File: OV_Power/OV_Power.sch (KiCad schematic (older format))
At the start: 41 parts, among them Q1 SSM3K341R, Q2 2N7002BK, U1 LT3796, U2 LT1936

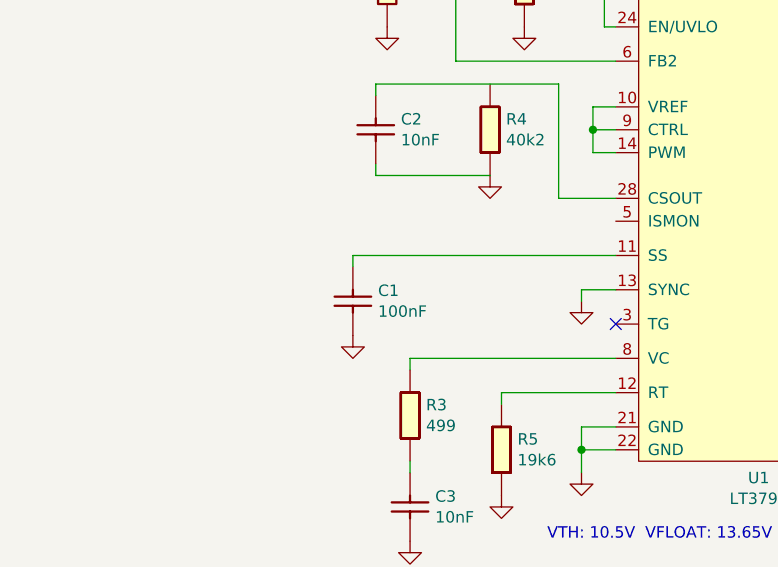
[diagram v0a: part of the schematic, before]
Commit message: Sorted out the interconnect between power supply and main boards.
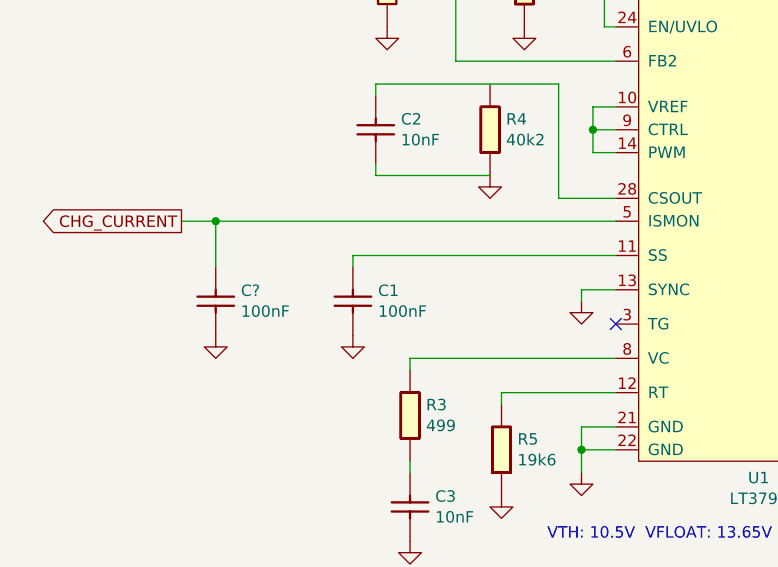
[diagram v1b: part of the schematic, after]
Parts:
- added C?: 100nF_0603_Ceramic_Capacitor,_10%,_X7R,_25V, Capacitor_SMD:C_0603_1608Metric, symbol OpenVent:100nF_0603_Ceramic_Capacitor,_10%,_X7R,_25V
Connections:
- net labels added: CHG_CURRENT
- wire segments 149 -> 152
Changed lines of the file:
@@
 Text Notes 10300 2000 0    50   ~ 0
 NEED CONNECTOR\nDEFINITION FOR\nGELL CELL.\nTHIS CONNECTION\nALSO NEEDS TO\nBE FUSED.
+$Comp
+L OpenVent:100nF_0603_Ceramic_Capacitor,_10%,_X7R,_25V C?
+U 1 1 5FB9582D
+P 2450 3100
+F 0 "C?" V 2454 3110 50  0000 L CNN
+F 1 "100nF_0603_Ceramic_Capacitor,_10%,_X7R,_25V" H 2450 3100 50  0001 C CNN
+F 2 "Capacitor_SMD:C_0603_1608Metric" H 2450 3100 50  0001 C CNN
+F 3 "" H 2450 3100 50  0001 C CNN
+F 4 "100nF" V 2545 3110 50  0000 L CNN "Val"
+F 5 "25V" H 2450 3100 50  0001 C CNN "Voltage"
+F 6 "10%" H 2450 3100 50  0001 C CNN "Tolerance"
+	1    2450 3100
+	0    1    1    0
+$EndComp
+$Comp
+L OpenVent:GND #GND_?
+U 1 1 5FB95C6B
+P 2350 3300
+F 0 "#GND_?" H 2350 3300 20  0001 C CNN
+F 1 "GND" H 2350 3230 30  0001 C CNN
+F 2 "" H 2350 3300 70  0000 C CNN
+F 3 "" H 2350 3300 70  0000 C CNN
+	1    2350 3300
+	1    0    0    -1
+$EndComp
+Wire Wire Line
+	4100 2800 2350 2800
+Wire Wire Line
+	2350 2800 2350 3000
+Text GLabel 2200 2800 0    50   Output ~ 0
+CHG_CURRENT
+Wire Wire Line
+	2350 2800 2200 2800
+Connection ~ 2350 2800
 $EndSCHEMATC

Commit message: First cut at a placement study for the power board.
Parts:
- C4: footprint (none) -> Capacitor_SMD:C_0603_1608Metric
- C5: value C -> C_0603_0.22uf_25V_10%; footprint (none) -> Capacitor_SMD:C_0603_1608Metric; symbol Device:C -> OpenVent:C_0603_0.22uf_25V_10%; Desc (none) -> CAP CER 0.22UF 25V X7R 0603; Detailed (none) -> 0.22µF ±10% 25V Ceramic Capacitor X7R 0603 (1608 Metric); Mfr (none) -> Murata Electronics; Mfr_PN (none) -> GCM188R71E224KA55J; Tol (none) -> 10%; Volt (none) -> 25V
- D2: value 1N4141 -> MMBD914; footprint (none) -> Package_TO_SOT_SMD:SOT-23; symbol Device:D -> OpenVent:MMBD914; Current (none) -> 200mA; Desc (none) -> DIODE GEN PURP 100V 200MA SOT23; Detailed (none) -> Diode Standard 100V 200mA Surface Mount SOT-23; Mfr (none) -> Vishay Semiconductor Diodes Division; Mfr_PN (none) -> MMBD914-E3-08; Volt (none) -> 100V
- L2: value L_Ferrite -> L_22uH_2.6A_42mOhm_SMT; footprint (none) -> F_Inductors:L-Bourns-SRU1048-series; symbol Device:L_Ferrite -> OpenVent:L_22uH_2.6A_42mOhm_SMT; Current (none) -> 2.6A; Desc (none) -> FIXED IND 22UH 2.6A 42 MOHM SMD; Detailed (none) -> 22µH Shielded Wirewound Inductor 2.6A 42mOhm Nonstandard wi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; Mfr (none) -> Bourns Inc.; Mfr_PN (none) -> SRU1048-220Y
- R12: value R -> R_0603_53K_0.1W_1%; footprint (none) -> Resistor_SMD:R_0603_1608Metric; symbol Device:R -> OpenVent:R_0603_53K_0.1W_1%; Desc (none) -> RES 53K OHM 1% 1/10W 0603; Detailed (none) -> 53 kOhms ±1% 0.1W, 1/10W Chip Resistor 0603 (1608 Metric) A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; Mfr (none) -> KOA Speer Electronics, Inc.; Mfr_PN (none) -> RN73H1JTTD5302F25; Tol (none) -> 1%; Val 52.5K -> 53k; Watt (none) -> 0.1W
- R13: value R -> 10k_0603_Chip_Resistor,_1%,_0.1W; footprint (none) -> Capacitor_SMD:C_0603_1608Metric; symbol Device:R -> OpenVent:10k_0603_Chip_Resistor,_1%,_0.1W; Tolerance (none) -> 1%; Val 10K -> 10k; Watt (none) -> 0.1W
- R8: footprint (none) -> Resistor_SMD:R_0603_1608Metric
- gave numbers to parts that had none: 1
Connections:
- wire segments 152 -> 153
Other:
- moved on the sheet: C9
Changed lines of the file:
@@
 L OpenVent:VBATT #PWR013
 U 1 1 5F8DD1CC
-P 10000 1000
-F 0 "#PWR013" H 10000 1000 50  0001 C CNN
-F 1 "VBATT" H 10000 1150 50  0000 C CNN
-F 2 "" H 10000 1000 50  0001 C CNN
-F 3 "" H 10000 1000 50  0001 C CNN
-	1    10000 1000
+P 8600 1000
+F 0 "#PWR013" H 8600 1000 50  0001 C CNN
+F 1 "VBATT" H 8600 1150 50  0000 C CNN
+F 2 "" H 8600 1000 50  0001 C CNN
+F 3 "" H 8600 1000 50  0001 C CNN
+	1    8600 1000
 	1    0    0    -1
 $EndComp
@@
 L OpenVent:GND #PWR014
 U 1 1 5F8DD1C7
-P 10150 1350
-F 0 "#PWR014" H 10150 1350 50  0001 C CNN
-F 1 "GND" H 10150 1280 50  0001 C CNN
-F 2 "" H 10150 1350 50  0001 C CNN
-F 3 "" H 10150 1350 50  0001 C CNN
-	1    10150 1350
+P 8750 1400
+F 0 "#PWR014" H 8750 1400 50  0001 C CNN
+F 1 "GND" H 8750 1330 50  0001 C CNN
+F 2 "" H 8750 1400 50  0001 C CNN
+F 3 "" H 8750 1400 50  0001 C CNN
+	1    8750 1400
 	1    0    0    -1
 $EndComp
@@
 L OpenVent:1uF_0603_Ceramic_Capacitor,_10%,_50V,_X5R C9
 U 1 1 5FD8DCEA
-P 10250 1150
-F 0 "C9" V 10254 1160 50  0000 L CNN
-F 1 "1uF_0603_Ceramic_Capacitor,_10%,_50V,_X5R" H 10250 1150 50  0001 C CNN
-F 2 "Capacitor_SMD:C_0603_1608Metric" H 10250 1150 50  0001 C CNN
-F 3 "" H 10250 1150 50  0001 C CNN
-F 4 "1uF" V 10345 1160 50  0000 L CNN "Val"
-F 5 "50V" H 10250 1150 50  0001 C CNN "Voltage"
-F 6 "10%" H 10250 1150 50  0001 C CNN "Tolerance"
-	1    10250 1150
+P 8850 1200
+F 0 "C9" V 8854 1210 50  0000 L CNN
+F 1 "1uF_0603_Ceramic_Capacitor,_10%,_50V,_X5R" H 8850 1200 50  0001 C CNN
+F 2 "Capacitor_SMD:C_0603_1608Metric" H 8850 1200 50  0001 C CNN
+F 3 "" H 8850 1200 50  0001 C CNN
+F 4 "1uF" V 8945 1210 50  0000 L CNN "Val"
+F 5 "50V" H 8850 1200 50  0001 C CNN "Voltage"
+F 6 "10%" H 8850 1200 50  0001 C CNN "Tolerance"
+	1    8850 1200
 	0    1    1    0
 $EndComp
@@
 F1 "Motor_Driver.sch" 50
 $EndSheet
-Connection ~ 10150 1050
-Wire Wire Line
-	10150 1050 10550 1050
-Wire Wire Line
-	10000 1000 10000 1050
-Connection ~ 10000 1050
-Wire Wire Line
-	10000 1050 10150 1050
+Connection ~ 8600 1050
 $Sheet
 S 9850 6150 1350 150
@@
 $EndSheet
 Wire Wire Line
-	8450 1050 10000 1050
+	8450 1050 8600 1050
 $Comp
 L OpenVent:LT1936 U2
@@
 F 0 "C4" V 4304 4860 50  0000 L CNN
 F 1 "100nF_0603_Ceramic_Capacitor,_10%,_X7R,_25V" H 4300 4850 50  0001 C CNN
-F 2 "" H 4300 4850 50  0001 C CNN
+F 2 "Capacitor_SMD:C_0603_1608Metric" H 4300 4850 50  0001 C CNN
 F 3 "" H 4300 4850 50  0001 C CNN
 F 4 "100nF" V 4395 4860 50  0000 L CNN "Val"
@@
 $EndComp
 $Comp
-L Device:L_Ferrite L2
+L OpenVent:L_22uH_2.6A_42mOhm_SMT L2
 U 1 1 5FB271FB
 P 5900 5450
 F 0 "L2" V 6125 5450 50  0000 C CNN
-F 1 "L_Ferrite" V 6034 5450 50  0001 C CNN
-F 2 "" H 5900 5450 50  0001 C CNN
-F 3 "~" H 5900 5450 50  0001 C CNN
+F 1 "L_22uH_2.6A_42mOhm_SMT" V 6034 5450 50  0001 C CNN
+F 2 "F_Inductors:L-Bourns-SRU1048-series" H 5900 5450 50  0001 C CNN
+F 3 "https://www.bourns.com/docs/Product-Datasheets/SRU1048.pdf" H 5900 5450 50  0001 C CNN
 F 4 "22uH" V 6034 5450 50  0000 C CNN "Val"
+F 5 "2.6A" H 5900 5450 50  0001 C CNN "Current"
+F 6 "FIXED IND 22UH 2.6A 42 MOHM SMD" H 5900 5450 50  0001 C CNN "Desc"
+F 7 "22µH Shielded Wirewound Inductor 2.6A 42mOhm Nonstandard with Ferrite core" H 5900 5450 50  0001 C CNN "Detailed"
+F 8 "Bourns Inc." H 5900 5450 50  0001 C CNN "Mfr"
+F 9 "SRU1048-220Y" H 5900 5450 50  0001 C CNN "Mfr_PN"
 	1    5900 5450
 	0    -1   -1   0
 $EndComp
 $Comp
-L Device:C C5
+L OpenVent:C_0603_0.22uf_25V_10% C5
 U 1 1 5FB29AAF
 P 5300 5250
 F 0 "C5" H 5415 5296 50  0000 L CNN
-F 1 "C" H 5415 5205 50  0001 L CNN
-F 2 "" H 5338 5100 50  0001 C CNN
-F 3 "~" H 5300 5250 50  0001 C CNN
+F 1 "C_0603_0.22uf_25V_10%" H 5415 5205 50  0001 L CNN
+F 2 "Capacitor_SMD:C_0603_1608Metric" H 5338 5100 50  0001 C CNN
+F 3 "https://search.murata.co.jp/Ceramy/image/img/A01X/G101/ENG/GCM188R71E224KA55-01.pdf" H 5300 5250 50  0001 C CNN
 F 4 "0.22uF" H 5415 5205 50  0000 L CNN "Val"
+F 5 "CAP CER 0.22UF 25V X7R 0603" H 5300 5250 50  0001 C CNN "Desc"
+F 6 "0.22µF ±10% 25V Ceramic Capacitor X7R 0603 (1608 Metric)" H 5300 5250 50  0001 C CNN "Detailed"
+F 7 "Murata Electronics" H 5300 5250 50  0001 C CNN "Mfr"
+F 8 "GCM188R71E224KA55J" H 5300 5250 50  0001 C CNN "Mfr_PN"
+F 9 "10%" H 5300 5250 50  0001 C CNN "Tol"
+F 10 "25V" H 5300 5250 50  0001 C CNN "Volt"
 	1    5300 5250
 	1    0    0    -1
 $EndComp
 $Comp
-L Device:R R12
+L OpenVent:R_0603_53K_0.1W_1% R12
 U 1 1 5FB2A48E
 P 6100 5650
 F 0 "R12" H 6170 5696 50  0000 L CNN
-F 1 "R" H 6170 5605 50  0001 L CNN
-F 2 "" V 6030 5650 50  0001 C CNN
-F 3 "~" H 6100 5650 50  0001 C CNN
-F 4 "52.5K" H 6170 5605 50  0000 L CNN "Val"
+F 1 "R_0603_53K_0.1W_1%" H 6170 5605 50  0001 L CNN
+F 2 "Resistor_SMD:R_0603_1608Metric" V 6030 5650 50  0001 C CNN
+F 3 "https://www.digikey.com/en/products/result?s=N4IgjCBcoLQCxVAYygMwIYBsDOBTANCAPZQDaIA7AAwCsAHAGwgC6hADgC5QggC%2B-QA" H 6100 5650 50  0001 C CNN
+F 4 "53k" H 6170 5605 50  0000 L CNN "Val"
+F 5 "RES 53K OHM 1% 1/10W 0603" H 6100 5650 50  0001 C CNN "Desc"
+F 6 "53 kOhms ±1% 0.1W, 1/10W Chip Resistor 0603 (1608 Metric) Automotive AEC-Q200, Moisture Resistant Metal Film" H 6100 5650 50  0001 C CNN "Detailed"
+F 7 "KOA Speer Electronics, Inc." H 6100 5650 50  0001 C CNN "Mfr"
+F 8 "RN73H1JTTD5302F25" H 6100 5650 50  0001 C CNN "Mfr_PN"
+F 9 "1%" H 6100 5650 50  0001 C CNN "Tol"
+F 10 "0.1W" H 6100 5650 50  0001 C CNN "Watt"
 	1    6100 5650
 	1    0    0    -1
 $EndComp
 $Comp
-L Device:D D2
+L OpenVent:MMBD914 D2
 U 1 1 5FB2B5F3
 P 5650 5050
 F 0 "D2" H 5650 5267 50  0000 C CNN
-F 1 "1N4141" H 5650 5176 50  0000 C CNN
-F 2 "" H 5650 5050 50  0001 C CNN
-F 3 "~" H 5650 5050 50  0001 C CNN
+F 1 "MMBD914" H 5650 5176 50  0000 C CNN
+F 2 "Package_TO_SOT_SMD:SOT-23" H 5650 5050 50  0001 C CNN
+F 3 "https://www.vishay.com/docs/85734/mmbd914.pdf" H 5650 5050 50  0001 C CNN
+F 4 "200mA" H 5650 5050 50  0001 C CNN "Current"
+F 5 "DIODE GEN PURP 100V 200MA SOT23" H 5650 5050 50  0001 C CNN "Desc"
+F 6 "Diode Standard 100V 200mA Surface Mount SOT-23" H 5650 5050 50  0001 C CNN "Detailed"
+F 7 "Vishay Semiconductor Diodes Division" H 5650 5050 50  0001 C CNN "Mfr"
+F 8 "MMBD914-E3-08" H 5650 5050 50  0001 C CNN "Mfr_PN"
+F 9 "100V" H 5650 5050 50  0001 C CNN "Volt"
 	1    5650 5050
 	1    0    0    -1
@@
 	6100 5450 6050 5450
 $Comp
-L Device:R R13
+L OpenVent:10k_0603_Chip_Resistor,_1%,_0.1W R13
 U 1 1 5FB44596
-P 6100 6050
-F 0 "R13" H 6170 6096 50  0000 L CNN
-F 1 "R" H 6170 6005 50  0001 L CNN
-F 2 "" V 6030 6050 50  0001 C CNN
-F 3 "~" H 6100 6050 50  0001 C CNN
-F 4 "10K" H 6170 6005 50  0000 L CNN "Val"
-	1    6100 6050
-	1    0    0    -1
+P 6200 6000
+F 0 "R13" V 6250 6000 50  0000 L CNN
+F 1 "10k_0603_Chip_Resistor,_1%,_0.1W" H 6270 5955 50  0001 L CNN
+F 2 "Capacitor_SMD:C_0603_1608Metric" V 6130 6000 50  0001 C CNN
+F 3 "~" H 6200 6000 50  0001 C CNN
+F 4 "10k" V 6350 6000 50  0000 L CNN "Val"
+F 5 "1%" H 6200 6000 50  0001 C CNN "Tolerance"
+F 6 "0.1W" H 6200 6000 50  0001 C CNN "Watt"
+	1    6200 6000
+	0    1    1    0
 $EndComp
 $Comp
@@
 L OpenVent:GND #PWR08
 U 1 1 5FB46FAF
-P 6100 6200
-F 0 "#PWR08" H 6100 5950 50  0001 C CNN
-F 1 "GND" H 6100 6050 50  0001 C CNN
-F 2 "" H 6100 6200 50  0001 C CNN
-F 3 "" H 6100 6200 50  0001 C CNN
-	1    6100 6200
+P 6100 6300
+F 0 "#PWR08" H 6100 6050 50  0001 C CNN
+F 1 "GND" H 6100 6150 50  0001 C CNN
+F 2 "" H 6100 6300 50  0001 C CNN
+F 3 "" H 6100 6300 50  0001 C CNN
+	1    6100 6300
 	1    0    0    -1
 $EndComp
@@
 F 0 "R8" V 4104 5570 50  0000 L CNN
 F 1 "100K_0603_Chip_Resistor,_1%,_0.1W" H 4050 5600 50  0001 C CNN
-F 2 "" H 4050 5600 50  0001 C CNN
+F 2 "Resistor_SMD:R_0603_1608Metric" H 4050 5600 50  0001 C CNN
 F 3 "" H 4050 5600 50  0001 C CNN
 F 4 "100k" V 4195 5570 50  0000 L CNN "Val"
@@
 NEED CONNECTOR\nDEFINITION FOR\nGELL CELL.\nTHIS CONNECTION\nALSO NEEDS TO\nBE FUSED.
 $Comp
-L OpenVent:100nF_0603_Ceramic_Capacitor,_10%,_X7R,_25V C?
+L OpenVent:100nF_0603_Ceramic_Capacitor,_10%,_X7R,_25V C14
 U 1 1 5FB9582D
 P 2450 3100
-F 0 "C?" V 2454 3110 50  0000 L CNN
+F 0 "C14" V 2454 3110 50  0000 L CNN
 F 1 "100nF_0603_Ceramic_Capacitor,_10%,_X7R,_25V" H 2450 3100 50  0001 C CNN
 F 2 "Capacitor_SMD:C_0603_1608Metric" H 2450 3100 50  0001 C CNN
@@
 $EndComp
 $Comp
-L OpenVent:GND #GND_?
+L OpenVent:GND #GND_018
 U 1 1 5FB95C6B
 P 2350 3300
-F 0 "#GND_?" H 2350 3300 20  0001 C CNN
+F 0 "#GND_018" H 2350 3300 20  0001 C CNN
 F 1 "GND" H 2350 3230 30  0001 C CNN
 F 2 "" H 2350 3300 70  0000 C CNN
@@
 	2350 2800 2200 2800
 Connection ~ 2350 2800
+Wire Wire Line
+	8600 1050 8600 1000
+Wire Wire Line
+	8600 1050 8750 1050
+Wire Wire Line
+	8750 1100 8750 1050
+Connection ~ 8750 1050
+Wire Wire Line
+	8750 1050 10550 1050
 $EndSCHEMATC

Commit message: Continuing to refine both the schemo and placement for the power supply board.  I think we have all the connectors we need now...
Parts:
- removed TP1, TP2: Test_Point_PTH, TestPoint:TestPoint_Pad_2.0x2.0mm, symbol OpenVent:Test_Point_PTH
- added F1: Polyfuse_10A, OpenVent:LF_16R1000G, symbol OpenVent:Polyfuse_10A
- added J4, J5: SpadeLug, F_Connectors:TE_1217861-1, symbol F_connectors:SpadeLug
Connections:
- wire segments 153 -> 155
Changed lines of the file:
@@
-$EndComp
-$Comp
-L OpenVent:Test_Point_PTH TP1
-U 1 1 5F8DD1A7
-P 10550 1050
-F 0 "TP1" H 10050 950 50  0000 L BNN
-F 1 "Test_Point_PTH" H 10550 1050 50  0001 C CNN
-F 2 "TestPoint:TestPoint_Pad_2.0x2.0mm" H 10550 1050 50  0001 C CNN
-F 3 "" H 10550 1050 50  0001 C CNN
-F 4 "" H 10050 1050 50  0000 C CNN "Val"
-	1    10550 1050
-	-1   0    0    1
-$EndComp
-$Comp
-L OpenVent:Test_Point_PTH TP2
-U 1 1 5F8DD1A6
-P 10550 1250
-F 0 "TP2" H 10050 1200 50  0000 L BNN
-F 1 "Test_Point_PTH" H 9950 1250 50  0001 C CNN
-F 2 "TestPoint:TestPoint_Pad_2.0x2.0mm" H 10550 1250 50  0001 C CNN
-F 3 "" H 10550 1250 50  0001 C CNN
-F 4 "" H 10050 1300 50  0000 C CNN "Val"
-	1    10550 1250
-	-1   0    0    1
 $EndComp
 $Comp
@@
 F 2 "Diode_SMD:D_SMA" H 8200 1050 50  0001 C CNN
 F 3 "https://www.diodes.com/assets/Datasheets/ds16003.pdf" H 8200 1050 50  0001 C CNN
-F 4 "S1M-13-F" V 2500 -1550 50  0001 C CNN "Mfr_PN"
-F 5 "1A" H 8300 900 50  0000 C CNN "Current"
-F 6 "1KV" H 8100 900 50  0000 C CNN "Voltage"
+F 4 "S1M-13-F" H 8200 900 50  0000 C CNN "Mfr_PN"
+F 5 "1A" H 8200 1050 50  0001 C CNN "Current"
+F 6 "1KV" H 8200 1050 50  0001 C CNN "Voltage"
 F 7 "DIODE GEN PURP 1KV 1A SMA" H 8200 1050 50  0001 C CNN "Desc"
 F 8 "DigiKey" H 8200 1050 50  0001 C CNN "DistName"
@@
 L OpenVent:GND #PWR015
 U 1 1 5F957C60
-P 10550 1300
-F 0 "#PWR015" H 10550 1050 50  0001 C CNN
-F 1 "GND" H 10550 1150 50  0001 C CNN
-F 2 "" H 10550 1300 50  0001 C CNN
-F 3 "" H 10550 1300 50  0001 C CNN
-	1    10550 1300
-	1    0    0    -1
-$EndComp
-Wire Wire Line
-	10550 1250 10550 1300
+P 10450 1550
+F 0 "#PWR015" H 10450 1300 50  0001 C CNN
+F 1 "GND" H 10450 1400 50  0001 C CNN
+F 2 "" H 10450 1550 50  0001 C CNN
+F 3 "" H 10450 1550 50  0001 C CNN
+	1    10450 1550
+	1    0    0    -1
+$EndComp
 $Comp
 L OpenVent:1uF_0603_Ceramic_Capacitor,_10%,_50V,_X5R C9
@@
 Wire Wire Line
 	3100 900  3100 1050
-Text Notes 10300 2000 0    50   ~ 0
+Text Notes 10250 2550 0    50   ~ 0
 NEED CONNECTOR\nDEFINITION FOR\nGELL CELL.\nTHIS CONNECTION\nALSO NEEDS TO\nBE FUSED.
 $Comp
@@
 Connection ~ 8750 1050
 Wire Wire Line
-	8750 1050 10550 1050
+	8750 1050 9100 1050
+$Comp
+L F_connectors:SpadeLug J4
+U 1 1 5FCBB8E9
+P 10750 1050
+F 0 "J4" H 10780 1096 50  0000 L CNN
+F 1 "SpadeLug" H 10780 1005 50  0000 L CNN
+F 2 "F_Connectors:TE_1217861-1" H 10750 1050 50  0001 L BNN
+F 3 "https://www.te.com/commerce/DocumentDelivery/DDEController?Action=srchrtrv&DocNm=1217861&DocType=Customer+Drawing&DocLang=English" H 10750 1050 50  0001 L BNN
+F 4 "TE Connectivity AMP Connectors" H 10750 1050 50  0001 L BNN "Mfr"
+F 5 "1217861-1" H 10750 1050 50  0001 L BNN "MfrPn"
+F 6 "A100452CT-ND" H 10750 1050 50  0001 L BNN "DK_pn"
+F 7 "CONN QC TAB 0.250 SOLDER" H 10750 1050 50  0001 L BNN "Desc"
+F 8 "0.250\" (6.35mm) Quick Connect Male  Solder Connector Non-Insulated" H 10750 1050 50  0001 L BNN "Detailed"
+	1    10750 1050
+	1    0    0    -1
+$EndComp
+$Comp
+L F_connectors:SpadeLug J5
+U 1 1 5FCBC350
+P 10750 1450
+F 0 "J5" H 10780 1496 50  0000 L CNN
+F 1 "SpadeLug" H 10780 1405 50  0000 L CNN
+F 2 "F_Connectors:TE_1217861-1" H 10750 1450 50  0001 L BNN
+F 3 "https://www.te.com/commerce/DocumentDelivery/DDEController?Action=srchrtrv&DocNm=1217861&DocType=Customer+Drawing&DocLang=English" H 10750 1450 50  0001 L BNN
+F 4 "TE Connectivity AMP Connectors" H 10750 1450 50  0001 L BNN "Mfr"
+F 5 "1217861-1" H 10750 1450 50  0001 L BNN "MfrPn"
+F 6 "A100452CT-ND" H 10750 1450 50  0001 L BNN "DK_pn"
+F 7 "CONN QC TAB 0.250 SOLDER" H 10750 1450 50  0001 L BNN "Desc"
+F 8 "0.250\" (6.35mm) Quick Connect Male  Solder Connector Non-Insulated" H 10750 1450 50  0001 L BNN "Detailed"
+	1    10750 1450
+	1    0    0    -1
+$EndComp
+Wire Wire Line
+	10550 1450 10450 1450
+Wire Wire Line
+	10450 1450 10450 1550
+$Comp
+L OpenVent:Polyfuse_10A F1
+U 1 1 5FCE2FD4
+P 9250 1050
+F 0 "F1" V 8935 1050 50  0000 C CNN
+F 1 "Polyfuse_10A" V 9350 1050 50  0001 C CNN
+F 2 "OpenVent:LF_16R1000G" H 9300 850 50  0001 L CNN
+F 3 "https://www.littelfuse.com/~/media/electronics/datasheets/resettable_ptcs/littelfuse_ptc_16r_datasheet.pdf.pdf" H 9250 1050 50  0001 C CNN
+F 4 "Littelfuse Inc." H 9250 1050 50  0001 C CNN "Mfr"
+F 5 "16R1000GMR" H 9250 1050 50  0001 C CNN "Mfr_PN"
+F 6 "PTC RESET FUSE 16V 10A RADIAL" H 9250 1050 50  0001 C CNN "Desc"
+F 7 "Polymeric PTC Resettable Fuse 16V 10A Ih Through Hole Radial, Disc" H 9250 1050 50  0001 C CNN "Detailed"
+F 8 "10A" V 9026 1050 50  0000 C CNN "Current"
+F 9 "16V" V 9117 1050 50  0000 C CNN "Voltage"
+	1    9250 1050
+	0    1    1    0
+$EndComp
+Wire Wire Line
+	9400 1050 10550 1050
 $EndSCHEMATC

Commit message: Added two connectors for cooling fans, re-jigged the motor current sensing circuit a bit, still needs a bit of work there.
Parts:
- removed D4: DIODE_GEN_PURP_1KV_1A_SMA, Diode_SMD:D_SMA, symbol OpenVent:DIODE_GEN_PURP_1KV_1A_SMA
- added D4: S1B, Diode_SMD:D_SMA, symbol OpenVent:S1B
- J4, J5: symbol F_connectors:SpadeLug -> OV_Power-rescue:SpadeLug-F_connectors
- L1: symbol F_inductors:MSD1260-333 -> OV_Power-rescue:MSD1260-333-F_inductors
- U1: symbol F_ICs:LT3796 -> OV_Power-rescue:LT3796-F_ICs
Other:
- note added: "STANDBY POWER CONSUMPTION:\nD4 reverse leakage: 1uA MAX\nU2 in shutdown: less than 1uA\nMotor control in standby: 15uA MAX\nPower Path control, no input, on battery: 17uA MAX\nTotal power supply static drain in shutdown: 33uA maximum."
- note added: "Static drain of U2 in shutdown mode is less than 1uA."
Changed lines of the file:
@@
 	-1   0    0    -1
-$EndComp
-$Comp
-L OpenVent:DIODE_GEN_PURP_1KV_1A_SMA D4
-U 1 1 5F8DD18B
-P 8200 1050
-F 0 "D4" H 8100 1200 50  0000 L BNN
-F 1 "DIODE_GEN_PURP_1KV_1A_SMA" H 8200 1050 50  0001 C CNN
-F 2 "Diode_SMD:D_SMA" H 8200 1050 50  0001 C CNN
-F 3 "https://www.diodes.com/assets/Datasheets/ds16003.pdf" H 8200 1050 50  0001 C CNN
-F 4 "S1M-13-F" H 8200 900 50  0000 C CNN "Mfr_PN"
-F 5 "1A" H 8200 1050 50  0001 C CNN "Current"
-F 6 "1KV" H 8200 1050 50  0001 C CNN "Voltage"
-F 7 "DIODE GEN PURP 1KV 1A SMA" H 8200 1050 50  0001 C CNN "Desc"
-F 8 "DigiKey" H 8200 1050 50  0001 C CNN "DistName"
-F 9 "S1M-FDITR-ND" H 8200 1050 50  0001 C CNN "Dist_PN"
-F 10 "Diodes Incorporated" H 8200 1050 50  0001 C CNN "Mfr"
-F 11 "Diode Standard 1A Surface Mount SMA" H 8200 1050 50  0001 C CNN "Detailed"
-	1    8200 1050
-	1    0    0    -1
 $EndComp
 Text Notes 3800 4200 0    50   ~ 0
@@
 $EndComp
 $Comp
-L F_ICs:LT3796 U1
+L OV_Power-rescue:LT3796-F_ICs U1
 U 1 1 5FAE7EAD
 P 4100 3800
@@
 $EndComp
 $Comp
-L F_inductors:MSD1260-333 L1
+L OV_Power-rescue:MSD1260-333-F_inductors L1
 U 1 1 5FB0C2C0
 P 5400 1050
@@
 $EndComp
 $Comp
-L F_inductors:MSD1260-333 L1
+L OV_Power-rescue:MSD1260-333-F_inductors L1
 U 2 1 5FB0D579
 P 6350 1300
@@
 $EndComp
 Wire Wire Line
-	7950 1050 7900 1050
-Wire Wire Line
 	7900 1050 7900 1200
 Connection ~ 7900 1050
@@
 F1 "PowerSupply.sch" 50
 $EndSheet
-Wire Wire Line
-	8450 1050 8600 1050
 $Comp
 L OpenVent:LT1936 U2
@@
 	8750 1050 9100 1050
 $Comp
-L F_connectors:SpadeLug J4
+L OV_Power-rescue:SpadeLug-F_connectors J4
 U 1 1 5FCBB8E9
 P 10750 1050
@@
 $EndComp
 $Comp
-L F_connectors:SpadeLug J5
+L OV_Power-rescue:SpadeLug-F_connectors J5
 U 1 1 5FCBC350
 P 10750 1450
@@
 Wire Wire Line
 	9400 1050 10550 1050
+Text Notes 3650 6150 0    50   ~ 0
+Static drain of U2 in shutdown mode is less than 1uA.
+$Comp
+L OpenVent:S1B D4
+U 1 1 5FDCD265
+P 8200 1050
+F 0 "D4" H 8200 833 50  0000 C CNN
+F 1 "S1B" H 8200 924 50  0000 C CNN
+F 2 "Diode_SMD:D_SMA" H 8200 1050 50  0001 C CNN
+F 3 "https://www.onsemi.com/pub/Collateral/S1M-D.pdf" H 8200 1050 50  0001 C CNN
+F 4 "ON Semiconductor" H 8200 1050 50  0001 C CNN "Mfr"
+F 5 "S1B" H 8200 1050 50  0001 C CNN "Mfr_PN"
+F 6 "DIODE GEN PURP 100V 1A SMA" H 8200 1050 50  0001 C CNN "Desc"
+F 7 "Diode Standard 100V 1A Surface Mount SMA (DO-214AC)" H 8200 1050 50  0001 C CNN "Detailed"
+F 8 "100V" H 8200 1050 50  0001 C CNN "Voltage"
+F 9 "1A" H 8200 1050 50  0001 C CNN "Current"
+	1    8200 1050
+	-1   0    0    1
+$EndComp
+Wire Wire Line
+	8350 1050 8600 1050
+Wire Wire Line
+	7900 1050 8050 1050
+Text Notes 8150 3050 0    50   ~ 0
+STANDBY POWER CONSUMPTION:\nD4 reverse leakage: 1uA MAX\nU2 in shutdown: less than 1uA\nMotor control in standby: 15uA MAX\nPower Path control, no input, on battery: 17uA MAX\nTotal power supply static drain in shutdown: 33uA maximum.
+Connection ~ 4700 1050
+Connection ~ 5100 1050
 $EndSCHEMATC
